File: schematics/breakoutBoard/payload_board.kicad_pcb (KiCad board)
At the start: 4 copper layers, 75 x 107 mm, 23 parts, among them P1 CONN_02X50, P2 CONN_02X50, P3 CONN_02X50, P4 CONN_02X50, U1 CBP, U2 TAMP, U3 CBP, U4 TAMP, U5 LAT-3, U6 TAMP

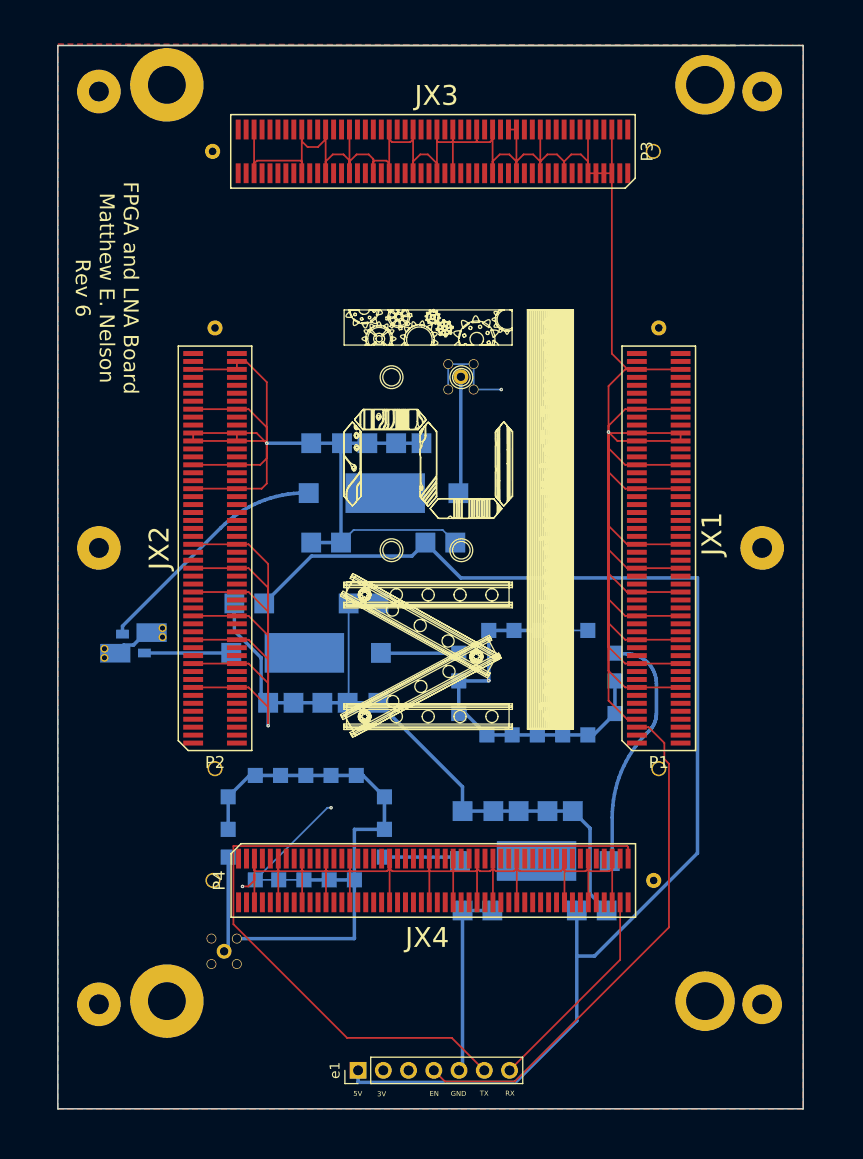
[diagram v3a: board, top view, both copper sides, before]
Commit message: Move files from main repo
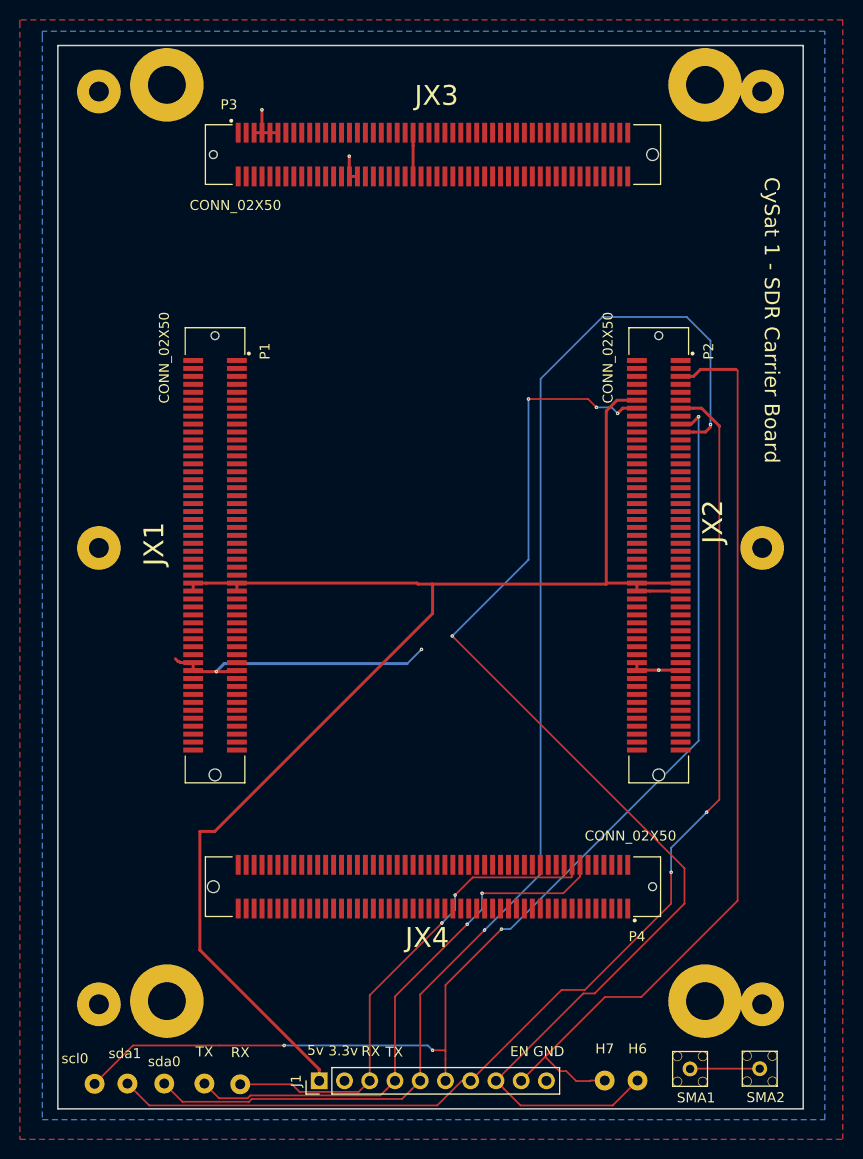
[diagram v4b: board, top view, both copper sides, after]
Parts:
- removed U1, U3: CBP, mini-circuits:CBP
- removed U2, U4, U6: TAMP, mini-circuits:MCL
- removed U5: LAT-3, RF_Mini-Circuits:Mini-Circuits_MMM168_LandPatternPL-225
- removed e1: ribbon2.54mmPitch, Connector_PinHeader_2.54mm:PinHeader_1x07_P2.54mm_Vertical
- added H6: MountingHole_Pad, MountingHole:MountingHole_2.2mm_M2_Pad, F.Cu at (108.3, 154.2)
- added H7: MountingHole_Pad, MountingHole:MountingHole_2.2mm_M2_Pad, F.Cu at (105.0, 154.2)
- added J1: Conn_01x10, Connector_PinHeader_2.54mm:PinHeader_1x10_P2.54mm_Vertical, F.Cu at (76.3, 154.2)
- added RX: MountingHole_Pad, MountingHole:MountingHole_2.2mm_M2_Pad, F.Cu at (68.4, 154.5)
- added TX: MountingHole_Pad, MountingHole:MountingHole_2.2mm_M2_Pad, F.Cu at (64.7, 154.5)
- added scl0: MountingHole_Pad, MountingHole:MountingHole_2.2mm_M2_Pad, F.Cu at (53.7, 154.5)
- added sda0: MountingHole_Pad, MountingHole:MountingHole_2.2mm_M2_Pad, F.Cu at (60.7, 154.5)
- added sda1: MountingHole_Pad, MountingHole:MountingHole_2.2mm_M2_Pad, F.Cu at (57.0, 154.5)
- P1, P2, P3, P4: footprint breakoutBoard:BERGSTAK_100_PIN1_RIGHT -> 61083-101400LF:FCI_61083-101400LF
- SMA1, SMA2: footprint breakoutBoard:Molex MMCX SMD 50Ohm -> Mounting_Holes:Molex MMCX SMD 50Ohm; moved to F.Cu
- moved SMA2 75.8 mm to (120.6, 153.0)
- moved SMA1 48.4 mm to (113.6, 153.0)
- moved P1 44.7 mm to (65.8, 101.3), turned to 270 degrees
- moved P2 44.7 mm to (110.5, 101.3), turned to 270 degrees
- moved P4 0.63 mm to (87.7, 134.6), turned to 180 degrees
- moved P3 0.32 mm to (87.7, 61.0), turned to 0 degrees
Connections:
- net 5V renamed /5v
- P1 pad 1: unconnected-(P1-Pad1) -> Net-(P1-Pad1)
- P1 pad 10: unconnected-(P1-Pad10) -> Net-(P1-Pad10)
- P1 pad 100: unconnected-(P1-Pad100) -> Net-(P1-Pad100)
- P1 pad 11: unconnected-(P1-Pad11) -> Net-(P1-Pad11)
- P1 pad 12: unconnected-(P1-Pad12) -> Net-(P1-Pad12)
- P1 pad 13: unconnected-(P1-Pad13) -> Net-(P1-Pad13)
- P1 pad 14: unconnected-(P1-Pad14) -> Net-(P1-Pad14)
- P1 pad 15: GND -> Net-(P1-Pad15)
- P1 pad 16: GND -> Net-(P1-Pad16)
- P1 pad 17: unconnected-(P1-Pad17) -> Net-(P1-Pad17)
- P1 pad 18: unconnected-(P1-Pad18) -> Net-(P1-Pad18)
- P1 pad 19: unconnected-(P1-Pad19) -> Net-(P1-Pad19)
- P1 pad 2: unconnected-(P1-Pad2) -> Net-(P1-Pad2)
- P1 pad 20: unconnected-(P1-Pad20) -> Net-(P1-Pad20)
- P1 pad 21: GND -> Net-(P1-Pad21)
- P1 pad 22: GND -> Net-(P1-Pad22)
- P1 pad 23: unconnected-(P1-Pad23) -> Net-(P1-Pad23)
- P1 pad 24: unconnected-(P1-Pad24) -> Net-(P1-Pad24)
- P1 pad 25: unconnected-(P1-Pad25) -> Net-(P1-Pad25)
- P1 pad 26: unconnected-(P1-Pad26) -> Net-(P1-Pad26)
- P1 pad 27: GND -> Net-(P1-Pad27)
- P1 pad 28: GND -> Net-(P1-Pad28)
- P1 pad 29: unconnected-(P1-Pad29) -> Net-(P1-Pad29)
- P1 pad 3: unconnected-(P1-Pad3) -> Net-(P1-Pad3)
- P1 pad 30: unconnected-(P1-Pad30) -> Net-(P1-Pad30)
- P1 pad 31: unconnected-(P1-Pad31) -> Net-(P1-Pad31)
- P1 pad 32: unconnected-(P1-Pad32) -> Net-(P1-Pad32)
- P1 pad 33: GND -> Net-(P1-Pad33)
- P1 pad 34: GND -> Net-(P1-Pad34)
- P1 pad 35: unconnected-(P1-Pad35) -> Net-(P1-Pad35)
- P1 pad 36: unconnected-(P1-Pad36) -> Net-(P1-Pad36)
- P1 pad 37: unconnected-(P1-Pad37) -> Net-(P1-Pad37)
- P1 pad 38: unconnected-(P1-Pad38) -> Net-(P1-Pad38)
- P1 pad 39: GND -> Net-(P1-Pad39)
- P1 pad 4: unconnected-(P1-Pad4) -> Net-(P1-Pad4)
- P1 pad 40: GND -> Net-(P1-Pad40)
- P1 pad 41: unconnected-(P1-Pad41) -> Net-(P1-Pad41)
- P1 pad 42: unconnected-(P1-Pad42) -> Net-(P1-Pad42)
- P1 pad 43: unconnected-(P1-Pad43) -> Net-(P1-Pad43)
- P1 pad 44: unconnected-(P1-Pad44) -> Net-(P1-Pad44)
- P1 pad 45: GND -> Net-(P1-Pad45)
- P1 pad 46: GND -> Net-(P1-Pad46)
- P1 pad 47: unconnected-(P1-Pad47) -> Net-(P1-Pad47)
- P1 pad 48: unconnected-(P1-Pad48) -> Net-(P1-Pad48)
- P1 pad 49: unconnected-(P1-Pad49) -> Net-(P1-Pad49)
- P1 pad 5: EN -> Net-(P1-Pad5)
- P1 pad 50: unconnected-(P1-Pad50) -> Net-(P1-Pad50)
- P1 pad 51: GND -> Net-(P1-Pad51)
- P1 pad 52: GND -> Net-(P1-Pad52)
- P1 pad 53: unconnected-(P1-Pad53) -> Net-(P1-Pad53)
- P1 pad 54: unconnected-(P1-Pad54) -> Net-(P1-Pad54)
- P1 pad 55: unconnected-(P1-Pad55) -> Net-(P1-Pad55)
- P1 pad 56: unconnected-(P1-Pad56) -> Net-(P1-Pad56)
- P1 pad 6: unconnected-(P1-Pad6) -> Net-(P1-Pad6)
- P1 pad 61: unconnected-(P1-Pad61) -> Net-(P1-Pad61)
- P1 pad 62: unconnected-(P1-Pad62) -> Net-(P1-Pad62)
- P1 pad 63: unconnected-(P1-Pad63) -> Net-(P1-Pad63)
- P1 pad 64: unconnected-(P1-Pad64) -> Net-(P1-Pad64)
- P1 pad 65: GND -> Net-(P1-Pad65)
- P1 pad 66: GND -> Net-(P1-Pad66)
- P1 pad 67: unconnected-(P1-Pad67) -> Net-(P1-Pad67)
- P1 pad 68: unconnected-(P1-Pad68) -> Net-(P1-Pad68)
- P1 pad 69: unconnected-(P1-Pad69) -> Net-(P1-Pad69)
- P1 pad 7: GND -> Net-(P1-Pad7)
- P1 pad 70: unconnected-(P1-Pad70) -> Net-(P1-Pad70)
- P1 pad 71: GND -> Net-(P1-Pad71)
- P1 pad 72: GND -> Net-(P1-Pad72)
- P1 pad 73: unconnected-(P1-Pad73) -> Net-(P1-Pad73)
- P1 pad 74: unconnected-(P1-Pad74) -> Net-(P1-Pad74)
- P1 pad 75: unconnected-(P1-Pad75) -> Net-(P1-Pad75)
- P1 pad 76: unconnected-(P1-Pad76) -> Net-(P1-Pad76)
- P1 pad 77: GND -> Net-(P1-Pad77)
- P1 pad 78: GND -> /3.3v
- P1 pad 79: GND -> /3.3v
- P1 pad 8: unconnected-(P1-Pad8) -> Net-(P1-Pad8)
- P1 pad 80: GND -> /3.3v
- P1 pad 81: unconnected-(P1-Pad81) -> Net-(P1-Pad81)
- P1 pad 82: unconnected-(P1-Pad82) -> Net-(P1-Pad82)
- P1 pad 83: unconnected-(P1-Pad83) -> Net-(P1-Pad83)
- P1 pad 84: unconnected-(P1-Pad84) -> Net-(P1-Pad84)
- P1 pad 85: GND -> Net-(P1-Pad85)
- P1 pad 86: GND -> Net-(P1-Pad86)
- P1 pad 87: unconnected-(P1-Pad87) -> Net-(P1-Pad87)
- P1 pad 88: unconnected-(P1-Pad88) -> Net-(P1-Pad88)
- P1 pad 89: unconnected-(P1-Pad89) -> Net-(P1-Pad89)
- P1 pad 9: unconnected-(P1-Pad9) -> Net-(P1-Pad9)
- P1 pad 90: unconnected-(P1-Pad90) -> Net-(P1-Pad90)
- P1 pad 91: unconnected-(P1-Pad91) -> Net-(P1-Pad91)
- P1 pad 92: unconnected-(P1-Pad92) -> Net-(P1-Pad92)
- P1 pad 93: unconnected-(P1-Pad93) -> Net-(P1-Pad93)
- P1 pad 94: unconnected-(P1-Pad94) -> Net-(P1-Pad94)
- P1 pad 95: GND -> Net-(P1-Pad95)
- P1 pad 96: GND -> Net-(P1-Pad96)
- P1 pad 97: unconnected-(P1-Pad97) -> Net-(P1-Pad97)
- P1 pad 98: unconnected-(P1-Pad98) -> Net-(P1-Pad98)
- P1 pad 99: unconnected-(P1-Pad99) -> Net-(P1-Pad99)
- P2 pad 1: unconnected-(P2-Pad1) -> Net-(P2-Pad1)
- P2 pad 10: unconnected-(P2-Pad10) -> Net-(P2-Pad10)
- P2 pad 100: unconnected-(P2-Pad100) -> Net-(P2-Pad100)
- P2 pad 11: unconnected-(P2-Pad11) -> Net-(P2-Pad11)
- P2 pad 13: unconnected-(P2-Pad13) -> /SDA1
- P2 pad 14: unconnected-(P2-Pad14) -> /SCL1
- P2 pad 15: GND -> Net-(P2-Pad15)
- P2 pad 16: GND -> Net-(P2-Pad16)
- P2 pad 17: unconnected-(P2-Pad17) -> /SCL0
- P2 pad 18: unconnected-(P2-Pad18) -> Net-(P2-Pad18)
- P2 pad 19: unconnected-(P2-Pad19) -> /SDA0
- P2 pad 2: unconnected-(P2-Pad2) -> Net-(P2-Pad2)
- P2 pad 20: unconnected-(P2-Pad20) -> Net-(P2-Pad20)
- P2 pad 21: GND -> Net-(P2-Pad21)
- P2 pad 22: GND -> Net-(P2-Pad22)
- P2 pad 23: unconnected-(P2-Pad23) -> Net-(P2-Pad23)
- P2 pad 24: unconnected-(P2-Pad24) -> Net-(P2-Pad24)
- P2 pad 25: unconnected-(P2-Pad25) -> Net-(P2-Pad25)
- P2 pad 26: unconnected-(P2-Pad26) -> Net-(P2-Pad26)
- P2 pad 27: GND -> Net-(P2-Pad27)
- P2 pad 28: GND -> Net-(P2-Pad28)
- P2 pad 29: unconnected-(P2-Pad29) -> Net-(P2-Pad29)
- P2 pad 3: unconnected-(P2-Pad3) -> Net-(P2-Pad3)
- P2 pad 30: unconnected-(P2-Pad30) -> Net-(P2-Pad30)
- P2 pad 31: unconnected-(P2-Pad31) -> Net-(P2-Pad31)
- P2 pad 32: unconnected-(P2-Pad32) -> Net-(P2-Pad32)
- P2 pad 33: GND -> Net-(P2-Pad33)
- P2 pad 34: GND -> Net-(P2-Pad34)
- P2 pad 35: unconnected-(P2-Pad35) -> Net-(P2-Pad35)
- P2 pad 36: unconnected-(P2-Pad36) -> Net-(P2-Pad36)
- P2 pad 37: unconnected-(P2-Pad37) -> Net-(P2-Pad37)
- P2 pad 38: unconnected-(P2-Pad38) -> Net-(P2-Pad38)
- P2 pad 39: GND -> Net-(P2-Pad39)
- P2 pad 4: unconnected-(P2-Pad4) -> Net-(P2-Pad4)
- P2 pad 40: GND -> Net-(P2-Pad40)
- P2 pad 41: unconnected-(P2-Pad41) -> Net-(P2-Pad41)
- P2 pad 42: unconnected-(P2-Pad42) -> Net-(P2-Pad42)
- P2 pad 43: unconnected-(P2-Pad43) -> Net-(P2-Pad43)
- P2 pad 44: unconnected-(P2-Pad44) -> Net-(P2-Pad44)
- P2 pad 45: GND -> Net-(P2-Pad45)
- P2 pad 46: GND -> Net-(P2-Pad46)
- P2 pad 47: unconnected-(P2-Pad47) -> Net-(P2-Pad47)
- P2 pad 48: unconnected-(P2-Pad48) -> Net-(P2-Pad48)
- P2 pad 49: unconnected-(P2-Pad49) -> Net-(P2-Pad49)
- P2 pad 5: unconnected-(P2-Pad5) -> /ENABLE
- P2 pad 50: unconnected-(P2-Pad50) -> Net-(P2-Pad50)
- P2 pad 51: GND -> Net-(P2-Pad51)
- P2 pad 52: GND -> Net-(P2-Pad52)
- P2 pad 53: unconnected-(P2-Pad53) -> Net-(P2-Pad53)
- P2 pad 54: unconnected-(P2-Pad54) -> Net-(P2-Pad54)
- P2 pad 55: unconnected-(P2-Pad55) -> Net-(P2-Pad55)
- P2 pad 56: unconnected-(P2-Pad56) -> Net-(P2-Pad56)
- P2 pad 6: unconnected-(P2-Pad6) -> Net-(P2-Pad6)
- P2 pad 61: unconnected-(P2-Pad61) -> Net-(P2-Pad61)
- P2 pad 62: unconnected-(P2-Pad62) -> Net-(P2-Pad62)
- P2 pad 63: unconnected-(P2-Pad63) -> Net-(P2-Pad63)
- P2 pad 64: unconnected-(P2-Pad64) -> Net-(P2-Pad64)
- P2 pad 65: GND -> Net-(P2-Pad65)
- P2 pad 66: GND -> Net-(P2-Pad66)
- P2 pad 67: unconnected-(P2-Pad67) -> Net-(P2-Pad67)
- P2 pad 68: unconnected-(P2-Pad68) -> Net-(P2-Pad68)
- P2 pad 69: unconnected-(P2-Pad69) -> Net-(P2-Pad69)
- P2 pad 7: unconnected-(P2-Pad7) -> Net-(P2-Pad7)
- P2 pad 70: unconnected-(P2-Pad70) -> Net-(P2-Pad70)
- P2 pad 71: GND -> Net-(P2-Pad71)
- P2 pad 72: GND -> Net-(P2-Pad72)
- P2 pad 73: unconnected-(P2-Pad73) -> Net-(P2-Pad73)
- P2 pad 74: unconnected-(P2-Pad74) -> Net-(P2-Pad74)
- P2 pad 75: unconnected-(P2-Pad75) -> Net-(P2-Pad75)
- P2 pad 76: unconnected-(P2-Pad76) -> Net-(P2-Pad76)
- P2 pad 77: GND -> Net-(P2-Pad77)
- P2 pad 78: GND -> /GND
- P2 pad 79: GND -> /GND
- P2 pad 8: unconnected-(P2-Pad8) -> Net-(P2-Pad8)
- P2 pad 80: GND -> /GND
- P2 pad 81: unconnected-(P2-Pad81) -> Net-(P2-Pad81)
- P2 pad 82: unconnected-(P2-Pad82) -> Net-(P2-Pad82)
- P2 pad 83: unconnected-(P2-Pad83) -> Net-(P2-Pad83)
- P2 pad 84: unconnected-(P2-Pad84) -> Net-(P2-Pad84)
- P2 pad 85: GND -> Net-(P2-Pad85)
- P2 pad 86: GND -> Net-(P2-Pad86)
- P2 pad 87: unconnected-(P2-Pad87) -> Net-(P2-Pad87)
- P2 pad 88: unconnected-(P2-Pad88) -> Net-(P2-Pad88)
- P2 pad 89: unconnected-(P2-Pad89) -> Net-(P2-Pad89)
- P2 pad 9: unconnected-(P2-Pad9) -> Net-(P2-Pad9)
- P2 pad 90: unconnected-(P2-Pad90) -> Net-(P2-Pad90)
- P2 pad 91: unconnected-(P2-Pad91) -> Net-(P2-Pad91)
- P2 pad 92: unconnected-(P2-Pad92) -> Net-(P2-Pad92)
- P2 pad 93: unconnected-(P2-Pad93) -> Net-(P2-Pad93)
- P2 pad 94: unconnected-(P2-Pad94) -> Net-(P2-Pad94)
- P2 pad 95: GND -> Net-(P2-Pad95)
- P2 pad 96: GND -> Net-(P2-Pad96)
- P2 pad 97: unconnected-(P2-Pad97) -> Net-(P2-Pad97)
- P2 pad 98: GND -> /3.3v
- P2 pad 99: unconnected-(P2-Pad99) -> Net-(P2-Pad99)
- P3 pad 1: unconnected-(P3-Pad1) -> Net-(P3-Pad1)
- P3 pad 10: unconnected-(P3-Pad10) -> Net-(P3-Pad10)
- P3 pad 100: unconnected-(P3-Pad100) -> Net-(P3-Pad100)
- P3 pad 11: GND -> /GND
- P3 pad 12: GND -> Net-(P3-Pad12)
- P3 pad 13: unconnected-(P3-Pad13) -> Net-(P3-Pad13)
- P3 pad 14: unconnected-(P3-Pad14) -> Net-(P3-Pad14)
- P3 pad 15: unconnected-(P3-Pad15) -> Net-(P3-Pad15)
- P3 pad 16: unconnected-(P3-Pad16) -> Net-(P3-Pad16)
- P3 pad 17: GND -> Net-(P3-Pad17)
- P3 pad 18: unconnected-(P3-Pad18) -> Net-(P3-Pad18)
- P3 pad 19: unconnected-(P3-Pad19) -> Net-(P3-Pad19)
- P3 pad 2: unconnected-(P3-Pad2) -> Net-(P3-Pad2)
- P3 pad 20: unconnected-(P3-Pad20) -> Net-(P3-Pad20)
- P3 pad 21: unconnected-(P3-Pad21) -> Net-(P3-Pad21)
- P3 pad 22: unconnected-(P3-Pad22) -> Net-(P3-Pad22)
- P3 pad 23: GND -> Net-(P3-Pad23)
- P3 pad 24: GND -> Net-(P3-Pad24)
- P3 pad 25: unconnected-(P3-Pad25) -> Net-(P3-Pad25)
- P3 pad 26: unconnected-(P3-Pad26) -> Net-(P3-Pad26)
- P3 pad 27: unconnected-(P3-Pad27) -> Net-(P3-Pad27)
- P3 pad 28: unconnected-(P3-Pad28) -> Net-(P3-Pad28)
- P3 pad 29: GND -> Net-(P3-Pad29)
- P3 pad 3: unconnected-(P3-Pad3) -> Net-(P3-Pad3)
- P3 pad 30: GND -> /GND
- P3 pad 31: unconnected-(P3-Pad31) -> Net-(P3-Pad31)
- P3 pad 32: GND -> /GND
- P3 pad 33: unconnected-(P3-Pad33) -> Net-(P3-Pad33)
- P3 pad 34: unconnected-(P3-Pad34) -> Net-(P3-Pad34)
- P3 pad 35: GND -> Net-(P3-Pad35)
- P3 pad 36: GND -> Net-(P3-Pad36)
- P3 pad 37: unconnected-(P3-Pad37) -> Net-(P3-Pad37)
- P3 pad 38: unconnected-(P3-Pad38) -> Net-(P3-Pad38)
- P3 pad 39: unconnected-(P3-Pad39) -> Net-(P3-Pad39)
- P3 pad 4: unconnected-(P3-Pad4) -> Net-(P3-Pad4)
- P3 pad 40: GND -> Net-(P3-Pad40)
- P3 pad 41: unconnected-(P3-Pad41) -> Net-(P3-Pad41)
- P3 pad 42: unconnected-(P3-Pad42) -> Net-(P3-Pad42)
- P3 pad 43: unconnected-(P3-Pad43) -> Net-(P3-Pad43)
- P3 pad 44: unconnected-(P3-Pad44) -> Net-(P3-Pad44)
- P3 pad 45: GND -> /3.3v
- P3 pad 46: GND -> /3.3v
- P3 pad 47: unconnected-(P3-Pad47) -> Net-(P3-Pad47)
- P3 pad 48: unconnected-(P3-Pad48) -> Net-(P3-Pad48)
- P3 pad 49: GND -> Net-(P3-Pad49)
- P3 pad 5: GND -> /GND
- P3 pad 50: GND -> Net-(P3-Pad50)
- P3 pad 51: unconnected-(P3-Pad51) -> Net-(P3-Pad51)
- P3 pad 52: unconnected-(P3-Pad52) -> Net-(P3-Pad52)
- P3 pad 53: unconnected-(P3-Pad53) -> Net-(P3-Pad53)
- P3 pad 54: unconnected-(P3-Pad54) -> Net-(P3-Pad54)
- P3 pad 55: GND -> Net-(P3-Pad55)
- P3 pad 56: GND -> Net-(P3-Pad56)
- P3 pad 57: unconnected-(P3-Pad57) -> Net-(P3-Pad57)
- P3 pad 58: unconnected-(P3-Pad58) -> Net-(P3-Pad58)
- P3 pad 59: unconnected-(P3-Pad59) -> Net-(P3-Pad59)
- P3 pad 6: GND -> Net-(P3-Pad6)
- P3 pad 60: unconnected-(P3-Pad60) -> Net-(P3-Pad60)
- P3 pad 61: GND -> Net-(P3-Pad61)
- P3 pad 62: GND -> Net-(P3-Pad62)
- P3 pad 63: unconnected-(P3-Pad63) -> Net-(P3-Pad63)
- P3 pad 64: unconnected-(P3-Pad64) -> Net-(P3-Pad64)
- P3 pad 65: GND -> Net-(P3-Pad65)
- P3 pad 66: unconnected-(P3-Pad66) -> Net-(P3-Pad66)
- P3 pad 67: unconnected-(P3-Pad67) -> Net-(P3-Pad67)
- P3 pad 68: unconnected-(P3-Pad68) -> Net-(P3-Pad68)
- P3 pad 69: unconnected-(P3-Pad69) -> Net-(P3-Pad69)
- P3 pad 7: GND -> /GND
- P3 pad 70: unconnected-(P3-Pad70) -> Net-(P3-Pad70)
- P3 pad 71: GND -> Net-(P3-Pad71)
- P3 pad 72: GND -> Net-(P3-Pad72)
- P3 pad 73: unconnected-(P3-Pad73) -> Net-(P3-Pad73)
- P3 pad 74: unconnected-(P3-Pad74) -> Net-(P3-Pad74)
- P3 pad 75: unconnected-(P3-Pad75) -> Net-(P3-Pad75)
- P3 pad 76: unconnected-(P3-Pad76) -> Net-(P3-Pad76)
- P3 pad 77: GND -> Net-(P3-Pad77)
- P3 pad 78: GND -> Net-(P3-Pad78)
- P3 pad 79: unconnected-(P3-Pad79) -> Net-(P3-Pad79)
- P3 pad 8: unconnected-(P3-Pad8) -> Net-(P3-Pad8)
- P3 pad 80: unconnected-(P3-Pad80) -> Net-(P3-Pad80)
- P3 pad 81: unconnected-(P3-Pad81) -> Net-(P3-Pad81)
- P3 pad 82: unconnected-(P3-Pad82) -> Net-(P3-Pad82)
- P3 pad 83: GND -> Net-(P3-Pad83)
- P3 pad 84: GND -> Net-(P3-Pad84)
- P3 pad 85: unconnected-(P3-Pad85) -> Net-(P3-Pad85)
- P3 pad 86: unconnected-(P3-Pad86) -> Net-(P3-Pad86)
- P3 pad 87: unconnected-(P3-Pad87) -> Net-(P3-Pad87)
- P3 pad 88: unconnected-(P3-Pad88) -> Net-(P3-Pad88)
- P3 pad 89: unconnected-(P3-Pad89) -> Net-(P3-Pad89)
- P3 pad 9: GND -> /GND
- P3 pad 90: unconnected-(P3-Pad90) -> Net-(P3-Pad90)
- P3 pad 91: unconnected-(P3-Pad91) -> Net-(P3-Pad91)
- P3 pad 92: unconnected-(P3-Pad92) -> Net-(P3-Pad92)
- P3 pad 93: unconnected-(P3-Pad93) -> Net-(P3-Pad93)
- P3 pad 94: unconnected-(P3-Pad94) -> Net-(P3-Pad94)
- P3 pad 95: GND -> Net-(P3-Pad95)
- P3 pad 96: GND -> Net-(P3-Pad96)
- P3 pad 97: unconnected-(P3-Pad97) -> Net-(P3-Pad97)
- P3 pad 98: unconnected-(P3-Pad98) -> Net-(P3-Pad98)
- P3 pad 99: unconnected-(P3-Pad99) -> Net-(P3-Pad99)
- P4 pad 1: unconnected-(P4-Pad1) -> Net-(P4-Pad1)
- P4 pad 10: unconnected-(P4-Pad10) -> Net-(P4-Pad10)
- P4 pad 100: unconnected-(P4-Pad100) -> Net-(P4-Pad100)
- P4 pad 11: GND -> Net-(P4-Pad11)
- P4 pad 12: GND -> Net-(P4-Pad12)
- P4 pad 13: unconnected-(P4-Pad13) -> Net-(P4-Pad13)
- P4 pad 14: unconnected-(P4-Pad14) -> /UART_TX
- P4 pad 15: unconnected-(P4-Pad15) -> Net-(P4-Pad15)
- P4 pad 16: unconnected-(P4-Pad16) -> /UART_RX
- P4 pad 17: GND -> Net-(P4-Pad17)
- P4 pad 18: GND -> Net-(P4-Pad18)
- P4 pad 19: unconnected-(P4-Pad19) -> Net-(P4-Pad19)
- P4 pad 2: unconnected-(P4-Pad2) -> Net-(P4-Pad2)
- P4 pad 20: unconnected-(P4-Pad20) -> Net-(P4-Pad20)
- P4 pad 21: unconnected-(P4-Pad21) -> Net-(P4-Pad21)
- P4 pad 22: unconnected-(P4-Pad22) -> Net-(P4-Pad22)
- P4 pad 23: GND -> Net-(P4-Pad23)
- P4 pad 24: GND -> Net-(P4-Pad24)
- P4 pad 25: unconnected-(P4-Pad25) -> Net-(P4-Pad25)
- P4 pad 26: unconnected-(P4-Pad26) -> Net-(P4-Pad26)
- P4 pad 27: unconnected-(P4-Pad27) -> Net-(P4-Pad27)
- P4 pad 28: unconnected-(P4-Pad28) -> Net-(P4-Pad28)
- P4 pad 29: GND -> Net-(P4-Pad29)
- P4 pad 3: unconnected-(P4-Pad3) -> Net-(P4-Pad3)
- P4 pad 30: GND -> Net-(P4-Pad30)
- P4 pad 31: unconnected-(P4-Pad31) -> Net-(P4-Pad31)
- P4 pad 32: unconnected-(P4-Pad32) -> Net-(P4-Pad32)
- P4 pad 33: unconnected-(P4-Pad33) -> Net-(P4-Pad33)
- P4 pad 34: unconnected-(P4-Pad34) -> Net-(P4-Pad34)
- P4 pad 35: unconnected-(P4-Pad35) -> Net-(P4-Pad35)
- P4 pad 36: unconnected-(P4-Pad36) -> Net-(P4-Pad36)
- P4 pad 37: unconnected-(P4-Pad37) -> Net-(P4-Pad37)
- P4 pad 38: unconnected-(P4-Pad38) -> Net-(P4-Pad38)
- P4 pad 39: GND -> Net-(P4-Pad39)
- P4 pad 4: unconnected-(P4-Pad4) -> Net-(P4-Pad4)
- P4 pad 40: GND -> Net-(P4-Pad40)
- P4 pad 41: unconnected-(P4-Pad41) -> Net-(P4-Pad41)
- P4 pad 42: unconnected-(P4-Pad42) -> Net-(P4-Pad42)
- P4 pad 43: unconnected-(P4-Pad43) -> Net-(P4-Pad43)
- P4 pad 44: unconnected-(P4-Pad44) -> Net-(P4-Pad44)
- P4 pad 45: unconnected-(P4-Pad45) -> Net-(P4-Pad45)
- P4 pad 46: unconnected-(P4-Pad46) -> Net-(P4-Pad46)
- P4 pad 47: unconnected-(P4-Pad47) -> Net-(P4-Pad47)
- P4 pad 48: unconnected-(P4-Pad48) -> Net-(P4-Pad48)
- P4 pad 49: GND -> Net-(P4-Pad49)
- P4 pad 5: GND -> Net-(P4-Pad5)
- P4 pad 50: GND -> Net-(P4-Pad50)
- P4 pad 51: unconnected-(P4-Pad51) -> Net-(P4-Pad51)
- P4 pad 52: unconnected-(P4-Pad52) -> Net-(P4-Pad52)
- P4 pad 53: unconnected-(P4-Pad53) -> Net-(P4-Pad53)
- P4 pad 54: unconnected-(P4-Pad54) -> Net-(P4-Pad54)
- P4 pad 55: GND -> Net-(P4-Pad55)
- P4 pad 56: GND -> Net-(P4-Pad56)
- P4 pad 57: unconnected-(P4-Pad57) -> Net-(P4-Pad57)
- P4 pad 58: unconnected-(P4-Pad58) -> Net-(P4-Pad58)
- P4 pad 59: unconnected-(P4-Pad59) -> Net-(P4-Pad59)
- P4 pad 6: GND -> Net-(P4-Pad6)
- P4 pad 60: unconnected-(P4-Pad60) -> Net-(P4-Pad60)
- P4 pad 61: GND -> Net-(P4-Pad61)
- P4 pad 62: GND -> Net-(P4-Pad62)
- P4 pad 63: unconnected-(P4-Pad63) -> Net-(P4-Pad63)
- P4 pad 64: unconnected-(P4-Pad64) -> Net-(P4-Pad64)
- P4 pad 65: GND -> Net-(P4-Pad65)
- P4 pad 66: GND -> Net-(P4-Pad66)
- P4 pad 67: unconnected-(P4-Pad67) -> Net-(P4-Pad67)
- P4 pad 68: unconnected-(P4-Pad68) -> Net-(P4-Pad68)
- P4 pad 69: unconnected-(P4-Pad69) -> Net-(P4-Pad69)
- P4 pad 7: unconnected-(P4-Pad7) -> Net-(P4-Pad7)
- P4 pad 70: unconnected-(P4-Pad70) -> Net-(P4-Pad70)
- P4 pad 71: GND -> Net-(P4-Pad71)
- P4 pad 72: GND -> Net-(P4-Pad72)
- P4 pad 73: unconnected-(P4-Pad73) -> Net-(P4-Pad73)
- P4 pad 74: unconnected-(P4-Pad74) -> Net-(P4-Pad74)
- P4 pad 75: unconnected-(P4-Pad75) -> Net-(P4-Pad75)
- P4 pad 76: unconnected-(P4-Pad76) -> Net-(P4-Pad76)
- P4 pad 77: unconnected-(P4-Pad77) -> Net-(P4-Pad77)
- P4 pad 78: unconnected-(P4-Pad78) -> Net-(P4-Pad78)
- P4 pad 79: unconnected-(P4-Pad79) -> Net-(P4-Pad79)
- P4 pad 8: unconnected-(P4-Pad8) -> Net-(P4-Pad8)
- P4 pad 80: unconnected-(P4-Pad80) -> Net-(P4-Pad80)
- P4 pad 81: unconnected-(P4-Pad81) -> Net-(P4-Pad81)
- P4 pad 82: unconnected-(P4-Pad82) -> Net-(P4-Pad82)
- P4 pad 83: GND -> Net-(P4-Pad83)
- P4 pad 84: GND -> Net-(P4-Pad84)
- P4 pad 85: unconnected-(P4-Pad85) -> Net-(P4-Pad85)
- P4 pad 86: unconnected-(P4-Pad86) -> Net-(P4-Pad86)
- P4 pad 87: unconnected-(P4-Pad87) -> Net-(P4-Pad87)
- P4 pad 88: unconnected-(P4-Pad88) -> Net-(P4-Pad88)
- P4 pad 89: GND -> Net-(P4-Pad89)
- P4 pad 9: unconnected-(P4-Pad9) -> Net-(P4-Pad9)
- P4 pad 90: GND -> Net-(P4-Pad90)
- P4 pad 91: unconnected-(P4-Pad91) -> Net-(P4-Pad91)
- P4 pad 92: unconnected-(P4-Pad92) -> Net-(P4-Pad92)
- P4 pad 93: unconnected-(P4-Pad93) -> Net-(P4-Pad93)
- P4 pad 94: unconnected-(P4-Pad94) -> Net-(P4-Pad94)
- P4 pad 95: GND -> Net-(P4-Pad95)
- P4 pad 96: GND -> Net-(P4-Pad96)
- P4 pad 97: unconnected-(P4-Pad97) -> Net-(P4-Pad97)
- P4 pad 98: TX -> Net-(P4-Pad98)
- P4 pad 99: RX -> Net-(P4-Pad99)
- SMA1 pad 1: /LNA Side/RF_SIG -> Net-(SMA1-Pad1)
- SMA2 pad 1: Net-(SMA2-Pad1) -> Net-(SMA1-Pad1)
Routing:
- net GND: track 847.7 -> 0.00 mm, vias 4 -> 0
- net /SDA0: track 0.00 -> 135.6 mm, vias 0 -> 2
- net RFGND: track 127.0 -> 0.00 mm, vias 3 -> 0
- net /SDA1: track 0.00 -> 119.4 mm, vias 0 -> 2
- net /SCL1: track 0.00 -> 118.0 mm, vias 0 -> 4
- net /SCL0: track 0.00 -> 117.2 mm, vias 0 -> 4
- net /ENABLE: track 0.00 -> 95.7 mm
- net RX: track 80.1 -> 0.00 mm
- net /UART_TX: track 0.00 -> 54.8 mm, vias 0 -> 2
- net EN: track 52.7 -> 0.00 mm
- net /UART_RX: track 0.00 -> 49.8 mm, vias 0 -> 2
- net /3.3v: track 0.00 -> 33.2 mm, vias 0 -> 2
- net Net-(U2-Pad5): track 25.0 -> 0.00 mm
- net Net-(U5-Pad2): track 24.8 -> 0.00 mm
- net TX: track 21.5 -> 0.00 mm
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- added copper zone on F.Cu, net /3.3v
- added copper zone on B.Cu, net /GND
- removed copper zone on F.Cu, net /5v
- removed copper zone on In1.Cu, net GND
- removed copper zone on In2.Cu, net RFGND
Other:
- copper layers 4 -> 2
- net class Default added: clearance 0.1778, trace_width 0.1778, via_dia 0.3556, via_drill 0.1016
- rule pad_to_mask_clearance: 0 -> 0.2
- board text added: "3.3v"
- board text added: "5v"
- board text added: "CySat 1 - SDR Carrier Board"
- board text removed: "3V"
- board text removed: "5V"
- board text removed: "FPGA and LNA Board Matthew E. Nelson Rev 6"
